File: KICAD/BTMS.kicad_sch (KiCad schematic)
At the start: 172 parts, among them J1 Batt_Ballance, J10 USB_C_Receptacle_4085, J2 AUX_Charge, J3 Battery_IO, J4 Power_Out, J6 DSKY, J7 PWR_SW, J8 ICSP, J9 Heater, Q1 SSM3K341R, Q10 DMN65D8L, Q11 FDN340P, Q2 DMN65D8L, Q3 SSM3K341R, Q4 FDN340P, Q6 FDN340P, Q8 DMN65D8L, Q9 FDN340P, SW1 PTS526, U1 ACS711xLCTR-25AB, U11 AON7522E, U12 AON7522E, U13 LM62CIM3/NOPB, U14 FAN3100TSX, U15 FAN3100TSX, U16 AON7522E, U17 dsPIC30F3011-PT, U18 FT230XQ, U2 AP33772, U3 IS281-4, U4 Q294700DSGR, U5 SCF4030-12-0X, U6 AONR21321, U7 ACS711xLCTR-25AB, U8 IS281-4, U9 IRS2184

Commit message: Rerouted board after making changes to schematic.
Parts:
- removed C13, C18, C41, C? (x3): 1uf 25v BF, Capacitor_SMD:C_0603_1608Metric, symbol Device:C
- removed C25, C? (x3): 10uf 25v BF, Capacitor_SMD:C_0805_2012Metric, symbol Device:C
- removed D1: BL4, LED_SMD:LED_0603_1608Metric, symbol Device:LED
- removed D12: Diode40V, Diode_SMD:D_0603_1608Metric, symbol Device:D
- removed D13, D15, D16, D19, D20, D24, D25, D5: D_Schottky40V, Diode_SMD:D_0603_1608Metric, symbol Device:D
- removed Q10, Q8: DMN65D8L, Package_TO_SOT_SMD:SOT-23, symbol Device:Q_NMOS_GSD
- removed Q11, Q4, Q6, Q9: FDN340P, Package_TO_SOT_SMD:SOT-23, symbol Device:Q_PMOS_GSD
- removed R10, R11, R14: 12, Resistor_SMD:R_0603_1608Metric, symbol Device:R
- removed R2, R30, R4, R?: 150, Resistor_SMD:R_0805_2012Metric_Pad1.20x1.40mm_HandSolder, symbol Device:R
- removed R21: 91K, Resistor_SMD:R_0603_1608Metric, symbol Device:R
- removed R26, R29, R9, R? (x2): 10K, Resistor_SMD:R_0603_1608Metric, symbol Device:R
- removed R?: 100, Resistor_SMD:R_0603_1608Metric, symbol Device:R
- removed R?: 1K, Resistor_SMD:R_0603_1608Metric, symbol Device:R
- removed U9: IRS2184, Package_SO:SOIC-8-1EP_3.9x4.9mm_P1.27mm_EP2.514x3.2mm_ThermalVias, symbol Driver_FET:IRS2184
- added C19, C44, C45: 0.1uf BF, Capacitor_SMD:C_0402_1005Metric, symbol Device:C
- added C24, C32, C43: 1uf 25v BF, Capacitor_SMD:C_0402_1005Metric, symbol Device:C
- added C37, C38, C49, C50, C52, C53, C54: 10uf 25v BF, Capacitor_SMD:C_0805_2012Metric, symbol Device:C
- added D1, D23: SBRT15U50SP5-13, Package_TO_SOT_SMD:TO-277B, symbol Device:D_Schottky_AAK
- added D10, D11, D28: D_Schottky40V, Diode_SMD:D_0603_1608Metric, symbol Device:D
- added D19, D20, D21, D22: Amber_LED, LED_SMD:LED_0603_1608Metric, symbol Device:LED
- added D29: 5V1, Diode_SMD:D_SOD-123, symbol Device:D_Zener
- added D30, D31, D32: Green_LED, LED_SMD:LED_0603_1608Metric, symbol Device:LED
- added D33: 15V, Diode_SMD:D_SOD-123, symbol Device:D_Zener
- added D5: LED_RED, LED_SMD:LED_0603_1608Metric, symbol Device:LED
- added L2: 4.7uH, inductorModel:IND_ASPI-4030S-4R7M-T, symbol pspice:INDUCTOR
- added L3, L4: 2.2uH Thin Film, Inductor_SMD:L_0805_2012Metric_Pad1.15x1.40mm_HandSolder, symbol pspice:INDUCTOR
- added Q3, Q7: BSS84-7-F, Package_TO_SOT_SMD:SOT-23, symbol Device:Q_PMOS_GSD
- added R19: 0R, Resistor_SMD:R_1206_3216Metric, symbol Device:R
- added R22, R24, R28, R52, R76, R77: 1K, Resistor_SMD:R_0603_1608Metric, symbol Device:R
- added R31, R55, R59: 150, Resistor_SMD:R_0805_2012Metric_Pad1.20x1.40mm_HandSolder, symbol Device:R
- added R37, R46, R50: 100, Resistor_SMD:R_0603_1608Metric, symbol Device:R
- added R42: 56K, Resistor_SMD:R_0603_1608Metric, symbol Device:R
- added R44: 31K6, Resistor_SMD:R_0603_1608Metric, symbol Device:R
- added R62, R72: 27R, Resistor_SMD:R_0603_1608Metric, symbol Device:R
- added R64, R66, R70, R73, R78: 10K*, Resistor_SMD:R_0603_1608Metric, symbol Device:R
- added R65, R67, R71, R74, R79: 1K*, Resistor_SMD:R_0603_1608Metric, symbol Device:R
- added RN10, RN6, RN7: 5K, Resistor_SMD:R_Array_Convex_4x0612, symbol Device:R_Pack04
- added RN12: 10K, Resistor_SMD:R_Array_Convex_4x0612, symbol Device:R_Pack04
- added U11: ISL95808HRZ, Package_DFN_QFN:DFN-8-1EP_2x2mm_P0.5mm_EP0.8x1.6mm, symbol New_Library:ISL95808HRZ
- added U18, U19: AP62250Z6, Package_TO_SOT_SMD:SOT-563, symbol Regulator_Switching:AP62250Z6
- added U22: MIC5504-3.3YM5, Package_TO_SOT_SMD:SOT-23-5, symbol Regulator_Linear:MIC5504-3.3YM5
- added U23, U24, U25, U26: DMP2240UDM, Package_TO_SOT_SMD:SOT-23-6, symbol New_Library:DMP2240UDM
- C1, C2, C3: footprint Capacitor_SMD:C_0603_1608Metric -> Capacitor_SMD:C_0402_1005Metric; DK_Detail_Page https://www.digikey.com/en/products/detail/kyocera-avx/KGF1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 -> https://www.digikey.com/en/products/detail/samsung-electro-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; Digi-Key_PN 478-KGF15AR71H104KTCT-ND -> 1276-1043-1-ND
- C10: renamed from C8; footprint Capacitor_SMD:C_0603_1608Metric -> Capacitor_SMD:C_0402_1005Metric; DK_Detail_Page https://www.digikey.com/en/products/detail/kyocera-avx/KGF1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 -> https://www.digikey.com/en/products/detail/samsung-electro-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; Digi-Key_PN 478-KGF15AR71H104KTCT-ND -> 1276-1043-1-ND
- C12, C14, C15, C17: renamed from C?; footprint Capacitor_SMD:C_0603_1608Metric -> Capacitor_SMD:C_0402_1005Metric; DK_Detail_Page https://www.digikey.com/en/products/detail/tdk-corporation/C1608X7R1E105K080AE/5809180 -> https://www.digikey.com/en/products/detail/tdk-corporation/C1005X5R1E105K050BE/7907739; Digi-Key_PN 445-173615-1-ND -> 445-175215-1-ND
- C13: renamed from C11; footprint Capacitor_SMD:C_0603_1608Metric -> Capacitor_SMD:C_0402_1005Metric; DK_Detail_Page https://www.digikey.com/en/products/detail/tdk-corporation/C1608X7R1E105K080AE/5809180 -> https://www.digikey.com/en/products/detail/tdk-corporation/C1005X5R1E105K050BE/7907739; Digi-Key_PN 445-173615-1-ND -> 445-175215-1-ND
- C16: renamed from C12; footprint Capacitor_SMD:C_0603_1608Metric -> Capacitor_SMD:C_0402_1005Metric; DK_Detail_Page https://www.digikey.com/en/products/detail/kyocera-avx/KGF1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 -> https://www.digikey.com/en/products/detail/samsung-electro-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; Digi-Key_PN 478-KGF15AR71H104KTCT-ND -> 1276-1043-1-ND
- C20: footprint Capacitor_SMD:C_0603_1608Metric -> Capacitor_SMD:C_0402_1005Metric; DK_Detail_Page https://www.digikey.com/en/products/detail/tdk-corporation/C1608X7R1E105K080AE/5809180 -> https://www.digikey.com/en/products/detail/tdk-corporation/C1005X5R1E105K050BE/7907739; Digi-Key_PN 445-173615-1-ND -> 445-175215-1-ND
- C21: renamed from C23; footprint Capacitor_SMD:C_0603_1608Metric -> Capacitor_SMD:C_0402_1005Metric; DK_Detail_Page https://www.digikey.com/en/products/detail/tdk-corporation/C1608X7R1E105K080AE/5809180 -> https://www.digikey.com/en/products/detail/tdk-corporation/C1005X5R1E105K050BE/7907739; Digi-Key_PN 445-173615-1-ND -> 445-175215-1-ND
- C22: renamed from C24; footprint Capacitor_SMD:C_0603_1608Metric -> Capacitor_SMD:C_0402_1005Metric; DK_Detail_Page https://www.digikey.com/en/products/detail/tdk-corporation/C1608X7R1E105K080AE/5809180 -> https://www.digikey.com/en/products/detail/tdk-corporation/C1005X5R1E105K050BE/7907739; Digi-Key_PN 445-173615-1-ND -> 445-175215-1-ND
- C23: renamed from C28; footprint Capacitor_SMD:C_0603_1608Metric -> Capacitor_SMD:C_0402_1005Metric; DK_Detail_Page https://www.digikey.com/en/products/detail/tdk-corporation/C1608X7R1E105K080AE/5809180 -> https://www.digikey.com/en/products/detail/tdk-corporation/C1005X5R1E105K050BE/7907739; Digi-Key_PN 445-173615-1-ND -> 445-175215-1-ND
- C26: renamed from C27; footprint Capacitor_SMD:C_0603_1608Metric -> Capacitor_SMD:C_0402_1005Metric; DK_Detail_Page https://www.digikey.com/en/products/detail/tdk-corporation/C1608X7R1E105K080AE/5809180 -> https://www.digikey.com/en/products/detail/tdk-corporation/C1005X5R1E105K050BE/7907739; Digi-Key_PN 445-173615-1-ND -> 445-175215-1-ND
- C27: renamed from C35; footprint Capacitor_SMD:C_0603_1608Metric -> Capacitor_SMD:C_0402_1005Metric; DK_Detail_Page https://www.digikey.com/en/products/detail/tdk-corporation/C1608X7R1E105K080AE/5809180 -> https://www.digikey.com/en/products/detail/tdk-corporation/C1005X5R1E105K050BE/7907739; Digi-Key_PN 445-173615-1-ND -> 445-175215-1-ND
- C28: renamed from C44; footprint Capacitor_SMD:C_0603_1608Metric -> Capacitor_SMD:C_0402_1005Metric; DK_Detail_Page https://www.digikey.com/en/products/detail/tdk-corporation/C1608X7R1E105K080AE/5809180 -> https://www.digikey.com/en/products/detail/tdk-corporation/C1005X5R1E105K050BE/7907739; Digi-Key_PN 445-173615-1-ND -> 445-175215-1-ND
- C29: renamed from C26; footprint Capacitor_SMD:C_0603_1608Metric -> Capacitor_SMD:C_0402_1005Metric; DK_Detail_Page https://www.digikey.com/en/products/detail/kyocera-avx/KGF1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 -> https://www.digikey.com/en/products/detail/samsung-electro-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; Digi-Key_PN 478-KGF15AR71H104KTCT-ND -> 1276-1043-1-ND
- C30: renamed from C29; footprint Capacitor_SMD:C_0603_1608Metric -> Capacitor_SMD:C_0402_1005Metric; DK_Detail_Page https://www.digikey.com/en/products/detail/tdk-corporation/C1608X7R1E105K080AE/5809180 -> https://www.digikey.com/en/products/detail/tdk-corporation/C1005X5R1E105K050BE/7907739; Digi-Key_PN 445-173615-1-ND -> 445-175215-1-ND
- C31, C33, C35, C36, C39, C41, C48, C51: renamed from C?; footprint Capacitor_SMD:C_0603_1608Metric -> Capacitor_SMD:C_0402_1005Metric; DK_Detail_Page https://www.digikey.com/en/products/detail/kyocera-avx/KGF1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 -> https://www.digikey.com/en/products/detail/samsung-electro-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; Digi-Key_PN 478-KGF15AR71H104KTCT-ND -> 1276-1043-1-ND
- C34: renamed from C30; footprint Capacitor_SMD:C_0603_1608Metric -> Capacitor_SMD:C_0402_1005Metric; DK_Detail_Page https://www.digikey.com/en/products/detail/tdk-corporation/C1608X7R1E105K080AE/5809180 -> https://www.digikey.com/en/products/detail/tdk-corporation/C1005X5R1E105K050BE/7907739; Digi-Key_PN 445-173615-1-ND -> 445-175215-1-ND
- C4: renamed from C6; footprint Capacitor_SMD:C_0603_1608Metric -> Capacitor_SMD:C_0402_1005Metric; DK_Detail_Page https://www.digikey.com/en/products/detail/tdk-corporation/C1608X7R1E105K080AE/5809180 -> https://www.digikey.com/en/products/detail/tdk-corporation/C1005X5R1E105K050BE/7907739; Digi-Key_PN 445-173615-1-ND -> 445-175215-1-ND
- C40: renamed from C34; footprint Capacitor_SMD:C_0603_1608Metric -> Capacitor_SMD:C_0402_1005Metric; DK_Detail_Page https://www.digikey.com/en/products/detail/tdk-corporation/C1608X7R1E105K080AE/5809180 -> https://www.digikey.com/en/products/detail/tdk-corporation/C1005X5R1E105K050BE/7907739; Digi-Key_PN 445-173615-1-ND -> 445-175215-1-ND
- C42: renamed from C38; footprint Capacitor_SMD:C_0603_1608Metric -> Capacitor_SMD:C_0402_1005Metric; DK_Detail_Page https://www.digikey.com/en/products/detail/tdk-corporation/C1608X7R1E105K080AE/5809180 -> https://www.digikey.com/en/products/detail/tdk-corporation/C1005X5R1E105K050BE/7907739; Digi-Key_PN 445-173615-1-ND -> 445-175215-1-ND
- C46: renamed from C40; footprint Capacitor_SMD:C_0603_1608Metric -> Capacitor_SMD:C_0402_1005Metric; DK_Detail_Page https://www.digikey.com/en/products/detail/kyocera-avx/KGF1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 -> https://www.digikey.com/en/products/detail/samsung-electro-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; Digi-Key_PN 478-KGF15AR71H104KTCT-ND -> 1276-1043-1-ND
- C47: renamed from C43; footprint Capacitor_SMD:C_0603_1608Metric -> Capacitor_SMD:C_0402_1005Metric; DK_Detail_Page https://www.digikey.com/en/products/detail/kyocera-avx/KGF1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 -> https://www.digikey.com/en/products/detail/samsung-electro-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; Digi-Key_PN 478-KGF15AR71H104KTCT-ND -> 1276-1043-1-ND
- C5: renamed from C9; footprint Capacitor_SMD:C_0603_1608Metric -> Capacitor_SMD:C_0402_1005Metric; DK_Detail_Page https://www.digikey.com/en/products/detail/kyocera-avx/KGF1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 -> https://www.digikey.com/en/products/detail/samsung-electro-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; Digi-Key_PN 478-KGF15AR71H104KTCT-ND -> 1276-1043-1-ND
- C55: renamed from C14; footprint Capacitor_SMD:C_0603_1608Metric -> Capacitor_SMD:C_0402_1005Metric; DK_Detail_Page https://www.digikey.com/en/products/detail/tdk-corporation/C1608X7R1E105K080AE/5809180 -> https://www.digikey.com/en/products/detail/tdk-corporation/C1005X5R1E105K050BE/7907739; Digi-Key_PN 445-173615-1-ND -> 445-175215-1-ND
- C56: renamed from C42; footprint Capacitor_SMD:C_0603_1608Metric -> Capacitor_SMD:C_0402_1005Metric; DK_Detail_Page https://www.digikey.com/en/products/detail/tdk-corporation/C1608X7R1E105K080AE/5809180 -> https://www.digikey.com/en/products/detail/tdk-corporation/C1005X5R1E105K050BE/7907739; Digi-Key_PN 445-173615-1-ND -> 445-175215-1-ND
- C57: renamed from C22; footprint Capacitor_SMD:C_0603_1608Metric -> Capacitor_SMD:C_0402_1005Metric; DK_Detail_Page https://www.digikey.com/en/products/detail/tdk-corporation/C1608X7R1E105K080AE/5809180 -> https://www.digikey.com/en/products/detail/tdk-corporation/C1005X5R1E105K050BE/7907739; Digi-Key_PN 445-173615-1-ND -> 445-175215-1-ND
- C6: renamed from C10; footprint Capacitor_SMD:C_0603_1608Metric -> Capacitor_SMD:C_0402_1005Metric; DK_Detail_Page https://www.digikey.com/en/products/detail/kyocera-avx/KGF1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 -> https://www.digikey.com/en/products/detail/samsung-electro-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; Digi-Key_PN 478-KGF15AR71H104KTCT-ND -> 1276-1043-1-ND
- C7: renamed from C5; footprint Capacitor_SMD:C_0603_1608Metric -> Capacitor_SMD:C_0402_1005Metric; DK_Detail_Page https://www.digikey.com/en/products/detail/kyocera-avx/KGF1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 -> https://www.digikey.com/en/products/detail/samsung-electro-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; Digi-Key_PN 478-KGF15AR71H104KTCT-ND -> 1276-1043-1-ND
- C8: renamed from C7; footprint Capacitor_SMD:C_0603_1608Metric -> Capacitor_SMD:C_0402_1005Metric; DK_Detail_Page https://www.digikey.com/en/products/detail/tdk-corporation/C1608X7R1E105K080AE/5809180 -> https://www.digikey.com/en/products/detail/tdk-corporation/C1005X5R1E105K050BE/7907739; Digi-Key_PN 445-173615-1-ND -> 445-175215-1-ND
- C9: renamed from C4; footprint Capacitor_SMD:C_0603_1608Metric -> Capacitor_SMD:C_0402_1005Metric; DK_Detail_Page https://www.digikey.com/en/products/detail/kyocera-avx/KGF1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 -> https://www.digikey.com/en/products/detail/samsung-electro-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; Digi-Key_PN 478-KGF15AR71H104KTCT-ND -> 1276-1043-1-ND
- D2: value BL3 -> LED_RED
- D24: renamed from D22; value D_Schottky_AAK -> SBRT15U50SP5-13; DK_Detail_Page https://www.digikey.com/en/products/detail/on-semiconductor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 -> https://www.digikey.com/en/products/detail/diodes-incorpora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; Digi-Key_PN FSV20100VCT-ND -> SBRT15U50SP5-13DICT-ND
- D3: value BL2 -> LED_RED
- D4: value BL1 -> LED_RED
- D9: renamed from D11; value VB_Stat -> LED_RED
- J1: footprint Connector_JST:JST_VH_B5PS-VH_1x05_P3.96mm_Horizontal -> Connector_JST:JST_EH_S5B-EH_1x05_P2.50mm_Horizontal
- R11: renamed from R?; DK_Detail_Page (none) -> https://www.digikey.com/en/products/detail/yageo/RC0603FR-0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; Digi-Key_PN (none) -> 311-100HRCT-ND
- R23: value 10K -> 1K; DK_Detail_Page https://www.digikey.com/en/products/detail/bourns-inc/CR060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 -> https://www.digikey.com/en/products/detail/yageo/RC0603FR-0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; Digi-Key_PN CR0603-FX-1002ELFCT-ND -> 311-1.00KHRCT-ND
- R27: value 10K -> 1K; DK_Detail_Page https://www.digikey.com/en/products/detail/rohm-semiconduct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 -> https://www.digikey.com/en/products/detail/yageo/RC0603FR-0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; Digi-Key_PN RHM10KDCT-ND -> 311-1.00KHRCT-ND
- R3: value 150 -> 27R; footprint Resistor_SMD:R_0805_2012Metric_Pad1.20x1.40mm_HandSolder -> Resistor_SMD:R_0603_1608Metric; DK_Detail_Page https://www.digikey.com/en/products/detail/koa-speer-electr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 -> https://www.digikey.com/en/products/detail/yageo/RC0603FR-1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; Digi-Key_PN 2019-RK73B2ATTD151JCT-ND -> 13-RC0603FR-1327RLCT-ND
- RN4, RN5, RN9: value 1K -> 5K; DK_Detail_Page https://www.digikey.com/en/products/detail/bourns-inc/CAY16-1001F4LF/2566504 -> https://www.digikey.com/en/products/detail/bourns-inc/CAY16-4991F4LF/2566602; Digi-Key_PN CAY16-1001F4LFCT-ND -> CAY16-4991F4LFCT-ND
- gave numbers to parts that had none: 2
- renumbered C45 to C11, C16 to C18, C32 to C25, D7 to D12, D8 to D13, D9 to D14, D10 to D15, D28 to D17, D17 to D18, D21 to D25, D23 to D26, D6 to D8, F2 to F1, F3 to F2, F1 to F3, FB4 to FB2, J7 to J10, J10 to J2, J2 to J3, J3 to J4, J4 to J5, J9 to J8, J8 to J9, Q1 to Q2, Q2 to Q5, Q3 to Q6, R5 to R1, R18 to R12, R24 to R13, R31 to R14, R32 to R15, R33 to R16, R7 to R17, R22 to R18, R6 to R2, R8 to R21, R12 to R33, R13 to R34, R25 to R35, R15 to R39, R1 to R4, R16 to R40, R17 to R41, R19 to R47, R20 to R48, RN6 to RN3, RN10 to RN8, U7 to U10, U11 to U12, U12 to U13, U16 to U15, U13 to U16, U15 to U17, U17 to U20, U18 to U21, U4 to U3, U1 to U4, U3 to U5, U5 to U6, U2 to U7, U6 to U9
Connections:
- net Pctrl_IN is gone; now on net LBatt_Cell_1: RN4.2 (R2.1)
- net +3.3VA: now also RN9.2 (R2.1), R46.1, U22.5 (VOUT); no longer C48.1, C51.1, U20.17 (AVDD)
- net +5C: now also RN11.8 (R1.2), C50.1, C53.1, L4.2, Q3.2 (S), R44.2; no longer C16.1, C46.2, C7.1, R23.1, RN11.6 (R3.2), RN4.5 (R4.2), RN9.1 (R1.1), RN9.2 (R2.1), RN9.4 (R4.1), U10.8 (VCC), U21.1 (VCCIO), U21.10 (VCC), U21.8 (3V3OUT), U21.9 (~{RESET}), U4.8 (VCC)
- net BCsense: now also R28.2; no longer RN4.6 (R3.2)
- net BTStrapSig: now also C19.2, D23.3 (K), U11.8 (PHASE); no longer C21.2
- net CH_Boost+: now also RN7.3 (R3.1)
- net CHctrl+: now also R22.1, RN7.4 (R4.1)
- net C_Fault: now also D18.1 (K), RN11.1 (R1.1), Q3.1 (G); no longer RN4.4 (R4.1)
- net C_Fault_In: now also RN11.7 (R2.2), Q3.3 (D); no longer R27.2
- net ChargeVoltage: now also R78.1, R79.1
- net ExtBus: now also RN11.4 (R4.1)
- net GND: now also C21.2, R27.2, R4.1, RN11.2 (R2.1), RN11.3 (R3.1), RN4.1 (R1.1), U8.15 (out1_E), C24.2, C32.2, C37.2, C38.2, C43.2, C49.2, C50.2, C52.2, C53.2, C54.2, D19.1 (K), D20.1 (K), D21.1 (K), D22.1 (K), D23.1 (A), D23.2 (A), D29.2 (A), D30.1 (K), D31.1 (K), D32.1 (K), R65.1, R67.1, R71.1, R74.1, R79.2, RN12.5 (R4.2), RN12.6 (R3.2), RN12.7 (R2.2), U11.4 (GND), U11.9 (PAD), U18.3 (GND), U19.3 (GND), U22.2 (GND); no longer R27.1, RN11.4 (R4.1), U8.2 (in1_C), U8.6 (in3_C)
- net Heat_CTRL: now also RN7.1 (R1.1)
- net HighCHfet: now also U11.1 (UGATE)
- net IntBus: now also C32.1, D33.1 (K), L2.1, Q7.2 (S), RN12.8 (R1.2); no longer RN11.8 (R1.2)
- net KeepAlive: now also D27.2 (A); no longer RN11.5 (R4.2)
- net LBatt_Cell_1: now also U8.13 (out2_E), R31.1, RN10.8 (R1.2), RN6.8 (R1.2), U23.6 (D1), U25.6 (D1); no longer D4.2 (A), U8.16 (out1_C)
- net LBatt_Cell_2: now also RN4.3 (R3.1), U8.11 (out3_E), R55.1, RN10.7 (R2.2), RN6.7 (R2.2), U23.4 (D2), U25.4 (D2); no longer D3.2 (A), R3.1, U8.14 (out2_C)
- net LBatt_Cell_3: now also RN4.4 (R4.1), U8.9 (out4_E), R59.1, RN10.6 (R3.2), RN6.6 (R3.2), U24.6 (D1), U26.6 (D1); no longer D2.2 (A), U8.12 (out3_C)
- net LBatt_Cell_4: now also RN10.5 (R4.2), RN6.5 (R4.2), U24.4 (D2), U26.4 (D2); no longer R4.1, U8.10 (out4_C)
- net LithCell_V1: now also R64.2, R65.2
- net LithCell_V2: now also R66.2, R67.2
- net LithCell_V3: now also R70.2, R71.2
- net LithCell_V4: now also R73.2, R74.2
- net LowCHfet: now also U11.5 (LGATE)
- net MCLR: now also R37.2
- net Mult_B1: now also RN2.1 (R1.1); no longer RN5.1 (R1.1)
- net Mult_B2: now also RN2.2 (R2.1); no longer RN5.2 (R2.1)
- net Mult_B3: now also RN2.3 (R3.1); no longer RN5.3 (R3.1)
- net Mult_B4: now also RN2.4 (R4.1); no longer RN5.4 (R4.1)
- net Mult_SEL: now also R3.1; no longer U20.12 (PWM2L/RE2)
- net PowerOutEnable: now also R23.2, RN7.2 (R2.1); no longer RN4.8 (R1.2)
- net PowerOutput: no longer D27.2 (A)
- net VBUS: now also D11.2 (A), R19.1, R78.2; no longer R17.1, U7.24 (VCC)
- net __PwrKey: no longer RN11.3 (R3.1)
- net at C31.1, D25.1 (K), U20.18 (~{MCLR}): now also R37.1
- net at J10.1, SW1.2 (B): now also C56.1, R52.2; no longer D26.1 (K)
- net SW_Signal: now reaches D26.2 (A)
- net SW_Signal: now also RN9.1 (R1.1); no longer C56.1
- net at C55.1: now also C54.1, R50.2, U22.1 (VIN), U22.3 (EN)
- net +5VP: now reaches C8.1, U7.20 (V5V)
- net at U15.4 (G): now also U14.5 (OUT)
- net at RN2.5 (R4.2): now also RN5.1 (R1.1), U5.7 (in4_A)
- net Power_EN: now reaches D27.1 (K)
- net Power_EN: now also D26.1 (K), D28.1 (K), D29.1 (K), RN12.3 (R3.1), U18.5 (EN), U19.5 (EN)
- net at RN2.8 (R1.2): now also RN5.4 (R4.1), U5.1 (in1_A); no longer D4.1 (K)
- net at RN2.7 (R2.2): now also RN5.3 (R3.1), U5.3 (in2_A); no longer D3.1 (K)
- net +3.3VP: now reaches C9.1, U7.12 (V3VD)
- net +3.3VP: now also C46.2, U21.1 (VCCIO), U21.10 (VCC), U21.8 (3V3OUT), U21.9 (~{RESET}), D28.2 (A)
- net at U4.7 (VIOUT): now also R28.1; no longer RN4.3 (R3.1)
- net at U5.12 (out3_C): now also RN6.3 (R3.1), U24.1 (G1); no longer RN2.3 (R3.1)
- net at U5.16 (out1_C): now also RN6.1 (R1.1), U23.1 (G1); no longer RN2.1 (R1.1)
- net +5P: now reaches F4.1
- net +5P: now also C21.1, RN9.4 (R4.1), U14.1 (VDD), U17.1 (VDD), C24.1, C43.1, C49.1, C52.1, L3.2, R24.2, R42.2, R50.1, U11.6 (VCC)
- net at RN9.5 (R4.2): now also D30.2 (A); no longer U8.7 (in4_A)
- net at RN9.6 (R3.2): now also D31.2 (A); no longer U8.5 (in3_A)
- net at RN9.7 (R2.2): now also D32.2 (A); no longer U8.3 (in2_A)
- net at U8.1 (in1_A): now also R77.1; no longer RN9.8 (R1.2)
- net at R17.2, U7.1 (ISENP): now also D1.3 (K); no longer F1.2
- net at D2.1 (K): now also RN4.8 (R1.2); no longer RN2.6 (R3.2)
- net ExtBus_RES: now reaches Q5.3 (D), U9.4 (G)
- net ExtBus_RES: now also RN11.5 (R4.2)
- removed net IntSwitched: D18.2 (A), U14.1 (VDD), U17.1 (VDD)
- net PO_EN: no longer names the net of D17.2 (A), Q5.1 (G)
- net PO_EN: now also R23.1, RN11.6 (R3.2); no longer RN4.1 (R1.1)
- net Pctrl_OUT: no longer names the net of RN4.7 (R2.2)
- net Pctrl_OUT: now also D3.1 (K); no longer RN11.1 (R1.1)
- net Pre_Charge renamed C_Switched
- net C_Switched: now also R62.2, R72.1
- net V_Bus_Stat renamed V_Switched
- net V_Switched: now also R76.2, R77.2; no longer R23.2
- new net: R3.2, U20.12 (PWM2L/RE2)
- new net: C48.1, C51.1, R46.2, U20.17 (AVDD)
- new net: C7.1, R62.1, U4.8 (VCC)
- new net: D15.1 (K), RN5.5 (R4.2)
- new net: D22.2 (A), RN7.8 (R1.2)
- new net: D33.2 (A), Q7.1 (G), R52.1, RN12.1 (R1.1)
- new net: C45.1, U19.4 (BST)
- new net: C45.2, L4.1, U19.2 (SW)
- new net: C16.1, R72.2, U10.8 (VCC)
- new net: D19.2 (A), RN7.5 (R4.2)
- new net: D20.2 (A), RN7.6 (R3.2)
- new net: D21.2 (A), RN7.7 (R2.2)
- new net: RN10.1 (R1.1), U25.1 (G1), U8.16 (out1_C)
- new net: RN10.2 (R2.1), U25.3 (G2), U8.14 (out2_C)
- new net: RN10.3 (R3.1), U26.1 (G1), U8.12 (out3_C)
- new net: RN10.4 (R4.1), U26.3 (G2), U8.10 (out4_C)
- new net: C37.1, C38.1, L2.2, U18.1 (VIN), U19.1 (VIN)
- new net: D5.2 (A), R59.2, U24.2 (S2)
- new net: RN6.4 (R4.1), U24.3 (G2), U5.10 (out4_C)
- new net: D4.2 (A), R55.2, U24.5 (S1)
- new net: D5.1 (K), RN4.5 (R4.2)
- new net: C19.1, U11.2 (BOOT)
- new net: D2.2 (A), R4.2, U23.5 (S1)
- new net: D10.2 (A), R17.1, R19.2
- new net: R24.1, R27.1, U11.7 (FCCM)
- new net: RN6.2 (R2.1), U23.3 (G2), U5.14 (out2_C)
- new net: RN2.6 (R3.2), RN5.2 (R2.1), U5.5 (in3_A)
- new net: R64.1, U25.5 (S1)
- new net: D18.2 (A), R22.2, U11.3 (PWM)
- new net: D10.1 (K), D11.1 (K), U7.24 (VCC)
- new net: C44.1, U18.4 (BST)
- new net: C44.2, L3.1, U18.2 (SW)
- new net: R73.1, U26.2 (S2)
- new net: R70.1, U26.5 (S1)
- new net: R42.1, RN12.2 (R2.1), U18.6 (FB)
- new net: R44.1, RN12.4 (R4.1), U19.6 (FB)
- new net: D3.2 (A), R31.2, U23.2 (S2)
- new net: D1.1 (A), D1.2 (A), F1.2
- new net: R66.1, U25.2 (S2)
- new net: D12.1 (K), RN5.8 (R1.2)
- new net: D13.1 (K), RN5.7 (R2.2)
- new net: D4.1 (K), RN4.6 (R3.2)
- new net: Q7.3 (D), RN9.8 (R1.2)
- new net: D14.1 (K), RN5.6 (R3.2)
- new net: U8.2 (in1_C), U8.3 (in2_A)
- new net: R76.1, U8.5 (in3_A)
- new net: U8.6 (in3_C), U8.7 (in4_A)
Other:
- note added: "AUX 5v"
- note added: "Analog 3.3v"
- note added: "Digital 3.3v"
- note added: "MAX 6v on Enable signal for AP62250Z6"
- note added: "Remove this 0 ohm resistor if USB charging is not desired."
- moved on the sheet: C1, C10, C11, C12, C14, C15, C17, C2, C21, C3, C4, C46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

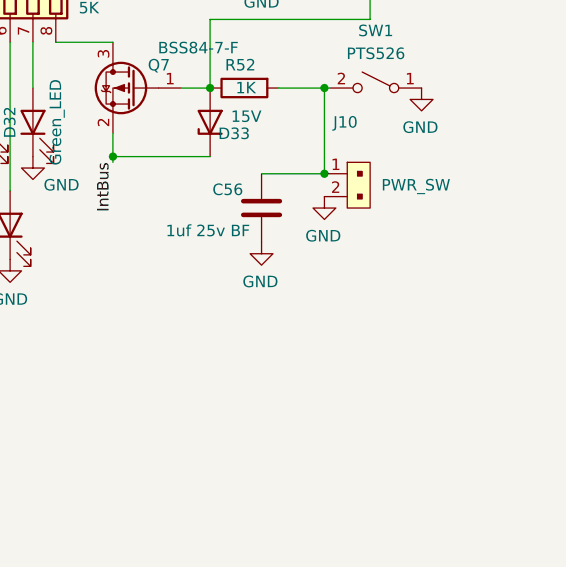
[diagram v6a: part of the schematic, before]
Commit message: Fixed power button not having a signal to dsPIC.
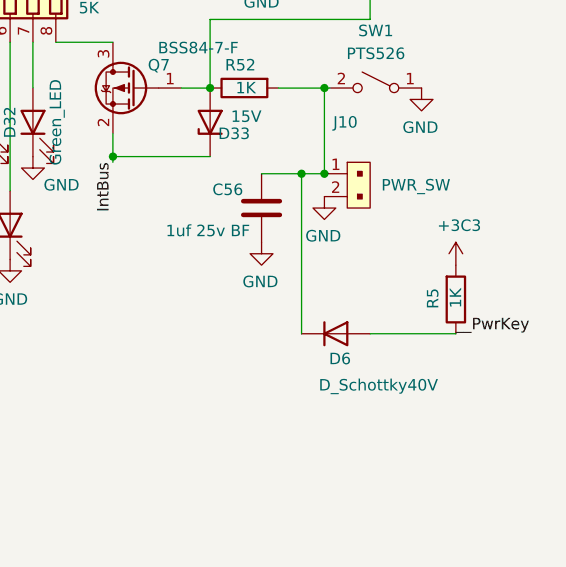
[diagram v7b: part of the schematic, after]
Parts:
- added D6: D_Schottky40V, Diode_SMD:D_0603_1608Metric, symbol Device:D
- added R5: 1K, Resistor_SMD:R_0603_1608Metric, symbol Device:R
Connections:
- net +5C: now also R5.2
- net __PwrKey: now also D6.2 (A), R5.1
- net at C56.1, J10.1, R52.2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: now also D6.1 (K)
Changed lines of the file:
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@@
   (junction (at 327.66 44.45) (diameter 0) (color 0 0 0 0)
   )
+  (junction (at 549.91 108.585) (diameter 0) (color 0 0 0 0)
+  )
   (junction (at 516.89 57.15) (diameter 0) (color 0 0 0 0)
   )
@@
     (stroke (width 0) (type default) (color 0 0 0 0))
   )
+  (wire (pts (xy 549.91 108.585) (xy 545.465 108.585))
+    (stroke (width 0) (type default) (color 0 0 0 0))
+  )
   (wire (pts (xy 414.655 238.76) (xy 421.005 238.76))
     (stroke (width 0) (type default) (color 0 0 0 0))
@@
     (stroke (width 0) (type default) (color 0 0 0 0))
   )
+  (wire (pts (xy 549.91 108.585) (xy 549.91 126.365))
+    (stroke (width 0) (type default) (color 0 0 0 0))
+  )
   (wire (pts (xy 269.875 321.31) (xy 269.875 325.12))
     (stroke (width 0) (type default) (color 0 0 0 0))
@@
     (stroke (width 0) (type default) (color 0 0 0 0))
   )
-  (wire (pts (xy 552.45 108.585) (xy 545.465 108.585))
+  (wire (pts (xy 552.45 108.585) (xy 549.91 108.585))
     (stroke (width 0) (type default) (color 0 0 0 0))
   )
@@
     (stroke (width 0) (type default) (color 0 0 0 0))
   )
+  (wire (pts (xy 557.53 126.365) (xy 567.055 126.365))
+    (stroke (width 0) (type default) (color 0 0 0 0))
+  )
   (wire (pts (xy 346.71 302.26) (xy 354.965 302.26))
     (stroke (width 0) (type default) (color 0 0 0 0))
@@
     (effects (font (size 1.27 1.27)) (justify left bottom))
   )
+  (label "__PwrKey" (at 567.055 126.365 0)
+    (effects (font (size 1.27 1.27)) (justify left bottom))
+  )
   (label "ChargeVoltage" (at 414.655 305.435 180)
     (effects (font (size 1.27 1.27)) (justify right bottom))
@@
     (pin "1")
   )
+  (symbol (lib_id "Device:D") (at 553.72 126.365 0) (unit 1)
+    (in_bom yes) (on_board yes)
+    (property "Reference" "D6" (id 0) (at 552.958 129.159 0)
+      (effects (font (size 1.27 1.27)) (justify left))
+    )
+    (property "Value" "D_Schottky40V" (id 1) (at 551.815 132.08 0)
+      (effects (font (size 1.27 1.27)) (justify left))
+    )
+    (property "Footprint" "Diode_SMD:D_0603_1608Metric" (id 2) (at 553.72 126.365 0)
+      (effects (font (size 1.27 1.27)) hide)
+    )
+    (property "Datasheet" "~" (id 3) (at 553.72 126.365 0)
+      (effects (font (size 1.27 1.27)) hide)
+    )
+    (property "DK_Detail_Page" "https://www.digikey.com/en/products/detail/toshiba-semiconductor-and-storage/CCS15S40L3F/5210646" (id 4) (at 553.72 126.365 0)
+      (effects (font (size 1.27 1.27)) hide)
+    )
+    (property "Digi-Key_PN" "CCS15S40L3FCT-ND" (id 5) (at 553.72 126.365 0)
+      (effects (font (size 1.27 1.27)) hide)
+    )
+    (pin "1")
+    (pin "2")
+  )
   (symbol (lib_id "Regulator_Linear:MIC5504-3.3YM5") (at 533.4 49.53 0) (unit 1)
     (in_bom yes) (on_board yes) (fields_autoplaced)
@@
     (pin "8")
   )
+  (symbol (lib_id "power:+5C") (at 567.055 118.745 0) (unit 1)
+    (in_bom yes) (on_board yes)
+    (property "Reference" "#PWR0114" (id 0) (at 567.055 122.555 0)
+      (effects (font (size 1.27 1.27)) hide)
+    )
+    (property "Value" "+3C3" (id 1) (at 567.436 114.3508 0))
+    (property "Footprint" "" (id 2) (at 567.055 118.745 0)
+      (effects (font (size 1.27 1.27)) hide)
+    )
+    (property "Datasheet" "" (id 3) (at 567.055 118.745 0)
+      (effects (font (size 1.27 1.27)) hide)
+    )
+    (pin "1")
+  )
   (symbol (lib_id "power:GND") (at 146.685 77.47 0) (unit 1)
     (in_bom yes) (on_board yes)
@@
     (pin "1")
   )
+  (symbol (lib_id "Device:R") (at 567.055 122.555 0) (mirror x) (unit 1)
+    (in_bom yes) (on_board yes)
+    (property "Reference" "R5" (id 0) (at 564.515 121.285 90)
+      (effects (font (size 1.27 1.27)) (justify left))
+    )
+    (property "Value" "1K" (id 1) (at 567.055 121.285 90)
+      (effects (font (size 1.27 1.27)) (justify left))
+    )
+    (property "Footprint" "Resistor_SMD:R_0603_1608Metric" (id 2) (at 565.277 122.555 90)
+      (effects (font (size 1.27 1.27)) hide)
+    )
+    (property "Datasheet" "~" (id 3) (at 567.055 122.555 0)
+      (effects (font (size 1.27 1.27)) hide)
+    )
+    (property "DK_Detail_Page" "https://www.digikey.com/en/products/detail/yageo/RC0603FR-071KL/726843" (id 4) (at 567.055 122.555 0)
+      (effects (font (size 1.27 1.27)) hide)
+    )
+    (property "Digi-Key_PN" "311-1.00KHRCT-ND" (id 5) (at 567.055 122.555 0)
+      (effects (font (size 1.27 1.27)) hide)
+    )
+    (pin "1")
+    (pin "2")
+  )
   (symbol (lib_id "power:GND") (at 322.58 73.66 0) (unit 1)
     (in_bom yes) (on_board yes)
@@
       (reference "#PWR0113") (unit 1) (value "+3.3VA") (footprint "")
     )
+    (path "/b439b67b-d429-451f-9d81-7caee2d989cd"
+      (reference "#PWR0114") (unit 1) (value "+3C3") (footprint "")
+    )
     (path "/00000000-0000-0000-0000-000060241ad7"
       (reference "#PWR0115") (unit 1) (value "+3C3") (footprint "")
@@
       (reference "D5") (unit 1) (value "LED_RED") (footprint "LED_SMD:LED_0603_1608Metric")
     )
+    (path "/96391b78-8f80-4b24-a916-5340d52e10c6"
+      (reference "D6") (unit 1) (value "D_Schottky40V") (footprint "Diode_SMD:D_0603_1608Metric")
+    )
     (path "/f207c2d2-ab77-438c-8c4d-b66a35772d19"
       (reference "D8") (unit 1) (value "D_Schottky40V") (footprint "Diode_SMD:D_0603_1608Metric")
@@
       (reference "R4") (unit 1) (value "150") (footprint "Resistor_SMD:R_0805_2012Metric_Pad1.20x1.40mm_HandSolder")
     )
+    (path "/cd949518-ec4d-4eb4-a0b3-857a5bae73f4"
+      (reference "R5") (unit 1) (value "1K") (footprint "Resistor_SMD:R_0603_1608Metric")
+    )
     (path "/9afeb565-8119-46ba-baa2-fce9d009db8e"

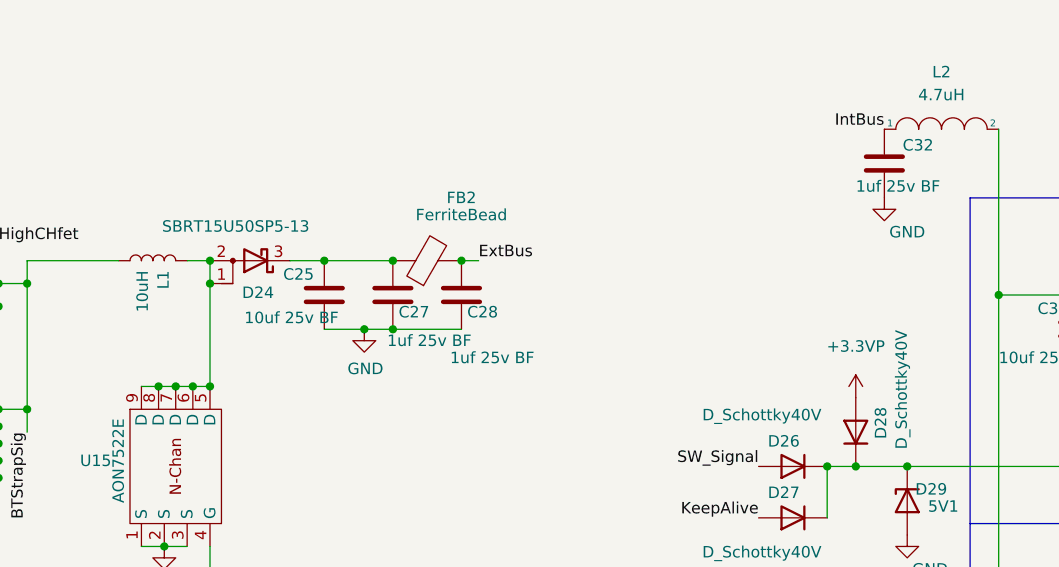
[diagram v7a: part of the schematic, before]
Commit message: Added four 10uF capacitors to ExtBus. Rerouted some things.
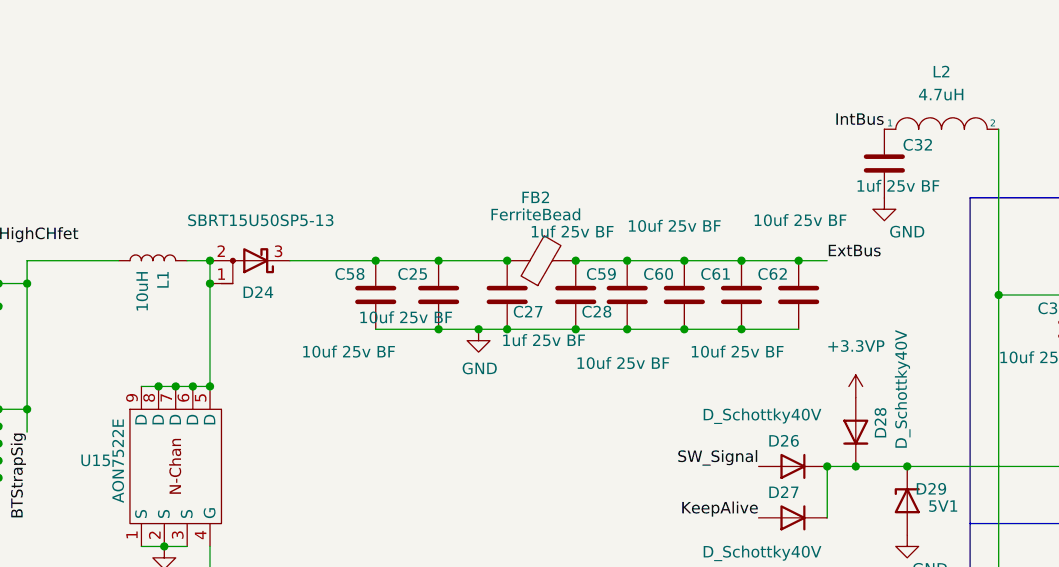
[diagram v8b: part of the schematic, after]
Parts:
- added C58, C59, C60, C61, C62: 10uf 25v BF, Capacitor_SMD:C_0805_2012Metric, symbol Device:C
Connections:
- net ExtBus: now also C59.1, C60.1, C61.1, C62.1
- net GND: now also C58.2, C59.2, C60.2, C61.2, C62.2
- net at C25.1, C27.1, D24.3 (K)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: now also C58.1
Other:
- moved on the sheet: C25, C27, C28, FB2
